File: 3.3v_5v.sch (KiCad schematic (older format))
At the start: 27 parts, among them J1 Jack-DC, SW1 SW_Push_SPDT, U1 AP1117-33, U6 MCP603-xCH

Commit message: update front endu do termopary i przełącznika zasilającego
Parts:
- added D7: D_Zener, Diode_SMD:D_0805_2012Metric_Castellated, symbol Device:D_Zener
- added Q2, Q3: AON7403, symbols:DFN_3X3_EP, symbol russian-nixies:AON7403
- added R10, R9: 100k, Resistor_SMD:R_0603_1608Metric, symbol Device:R
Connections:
- net 12v: now also Q3.1 (S), Q3.2 (S), Q3.3 (S); no longer SW1.2 (B), SW1.3 (C)
- net GND: now also SW1.3 (C)
- net at J1.1: now also Q2.5 (D), Q2.6 (D), Q2.7 (D), Q2.8 (D); no longer SW1.1 (A)
- new net: R10.2, R9.2, SW1.2 (B)
- new net: D7.1 (K), Q2.1 (S), Q2.2 (S), Q2.3 (S), Q3.5 (D), Q3.6 (D), Q3.7 (D), Q3.8 (D), R9.1
- new net: D7.2 (A), Q2.4 (G), Q3.4 (G), R10.1
- no-connect marks 0 -> 1
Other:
- note added: "dobrać"
- note added: "wzorowane na PololuMini MOSFET Slide Switch with Reverse Voltage Protection, SV\n"
- moved on the sheet: C1, C2, C21, C22, C23, C24, C27, C28, C29, C3, C30, C31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

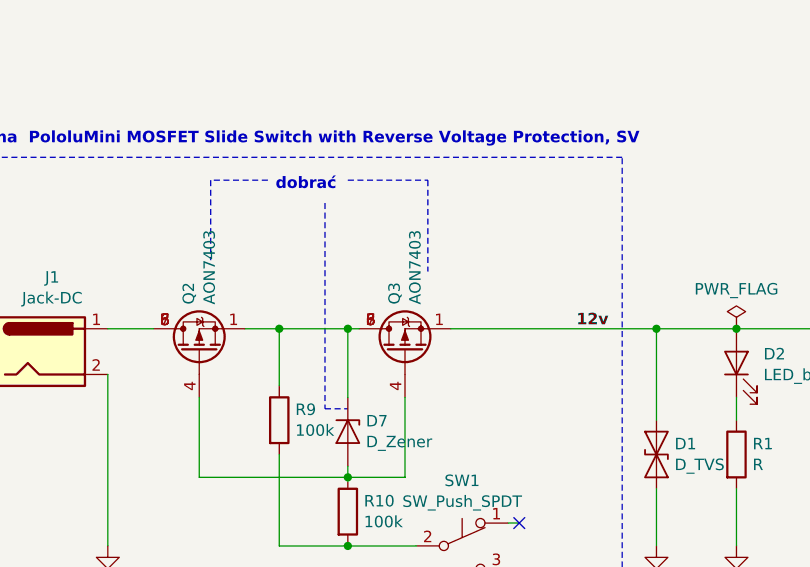
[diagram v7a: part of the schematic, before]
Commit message: update błędnego podpięcia pmosa na wejściu do układu, oras software testujący oled, przyciski i ledy
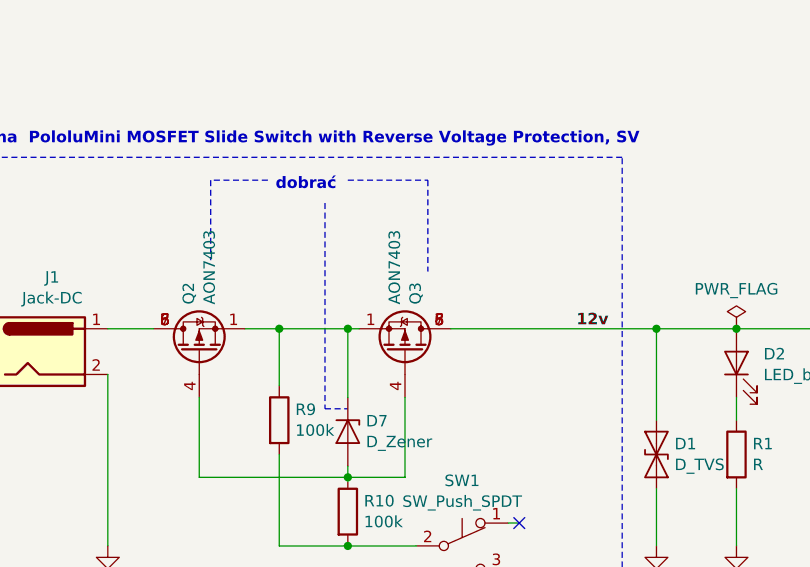
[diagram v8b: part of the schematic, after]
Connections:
- net 12v: now also Q3.5 (D), Q3.6 (D), Q3.7 (D), Q3.8 (D); no longer Q3.1 (S), Q3.2 (S), Q3.3 (S)
- net at D7.1 (K), Q2.1 (S), Q2.2 (S)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: now also Q3.1 (S), Q3.2 (S), Q3.3 (S); no longer Q3.5 (D), Q3.6 (D), Q3.7 (D), Q3.8 (D)
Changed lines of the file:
@@
 Wire Wire Line
 	8450 2550 8600 2550
-Text HLabel 10250 2550 2    50   Output ~ 6
+Text HLabel 10250 2550 2    50   Output ~ 10
 3.3v
 $Comp
@@
 Wire Wire Line
 	6100 1150 6350 1150
-Text HLabel 7150 5550 2    50   Output ~ 6
+Text HLabel 7150 5550 2    50   Output ~ 10
 input_v_sense
 $Comp
@@
 	1    0    0    -1
 $EndComp
-Text Label 3650 5100 0    50   ~ 6
+Text Label 3650 5100 0    50   ~ 10
 12v
 Wire Wire Line
 	3650 5100 3900 5100
-Text HLabel 6000 6450 3    50   Output ~ 6
+Text HLabel 6000 6450 3    50   Output ~ 10
 3.3v
-Text HLabel 5650 5200 1    50   Output ~ 6
+Text HLabel 5650 5200 1    50   Output ~ 10
 3.3v
-Text Notes 4100 4950 0    50   ~ 6
+Text Notes 4100 4950 0    50   ~ 10
 20V input = 3.3 v output
 Wire Notes Line
@@
 Wire Wire Line
 	5950 2300 5950 2550
-Text HLabel 6100 2300 2    50   Output ~ 6
+Text HLabel 6100 2300 2    50   Output ~ 10
 12v
 Wire Wire Line
@@
 Wire Wire Line
 	4650 2550 5000 2550
-Text Notes 3250 1950 2    50   ~ 6
+Text Notes 3250 1950 2    50   ~ 10
 dobrać
 Wire Wire Line
@@
 	3300 3500 3600 3500
 Connection ~ 3300 3500
-Text Label 4300 2550 0    50   ~ 6
+Text Label 4300 2550 0    50   ~ 10
 12v
 Wire Wire Line
@@
 	4000 3400 4050 3400
 NoConn ~ 4050 3400
-Text Notes 1300 1750 0    50   ~ 6
+Text Notes 1300 1750 0    50   ~ 10
 wzorowane na  PololuMini MOSFET Slide Switch with Reverse Voltage Protection, SV\n
 Wire Notes Line
@@
 F 3 "https://www.diodes.com/assets/Datasheets/DMP3013SFV.pdf" V 3550 2650 50  0001 L CNN
 	1    3550 2650
-	0    -1   -1   0
+	0    1    -1   0
 $EndComp
 $EndSCHEMATC
